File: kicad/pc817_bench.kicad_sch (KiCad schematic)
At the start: 27 parts, among them J1 24V, e-stops, lidars, U1 PC817, U2 PC817, U3 PC817, U4 PC817

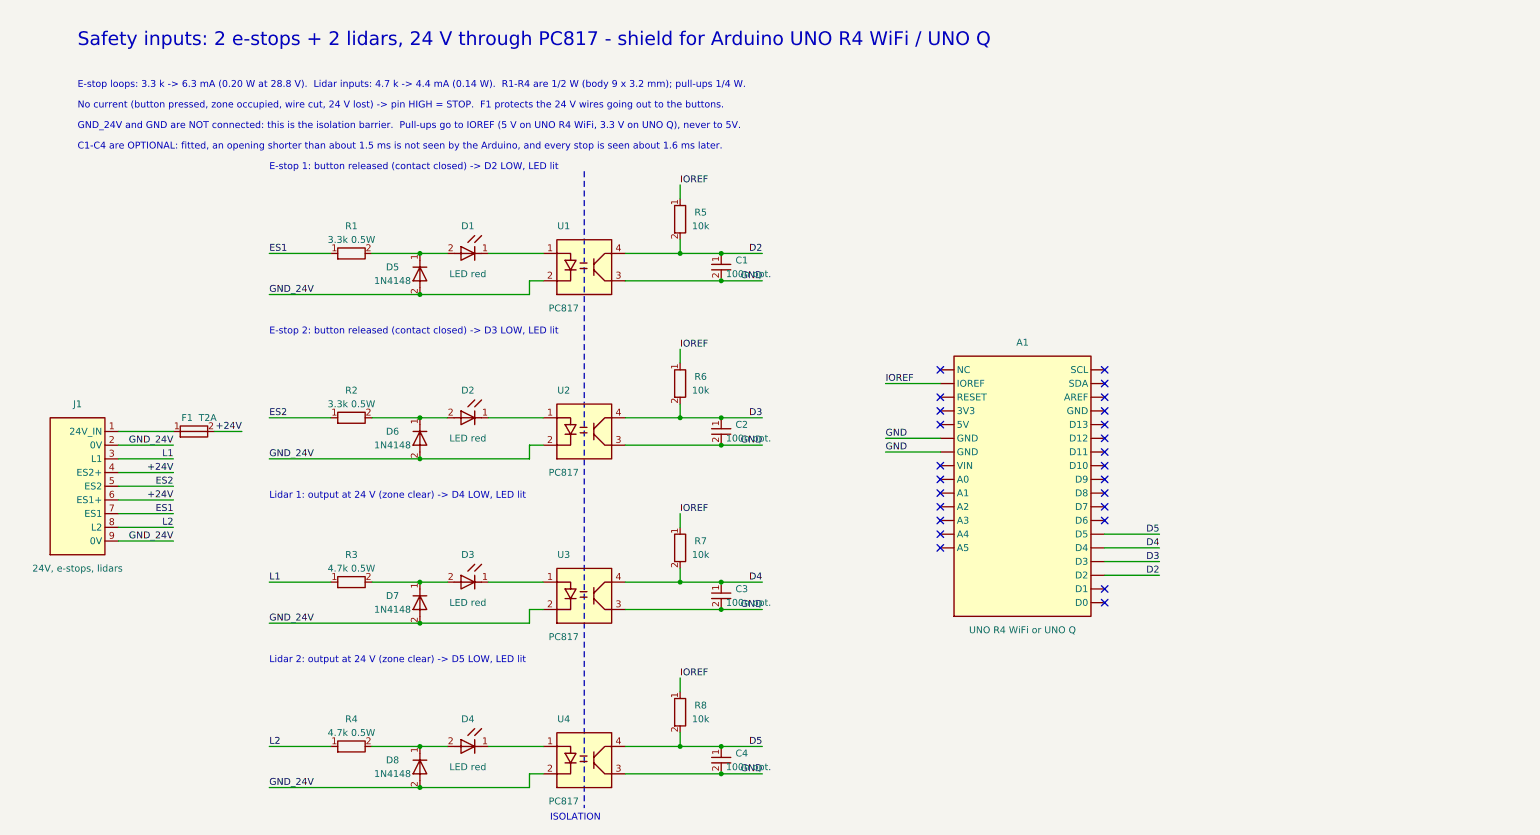
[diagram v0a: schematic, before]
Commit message: Schematic: draw the two external e-stop buttons and how they wire to the terminals
S1 (front) between ES1+ and ES1, S2 (rear) between ES2+ and ES2, in a dashed
box marked as external. Graphics only: no change to the netlist or the board.
The sheet content is shifted right to make room.

Co-Authored-By: Claude Fable 5.1 <noreply@anthropic.com>
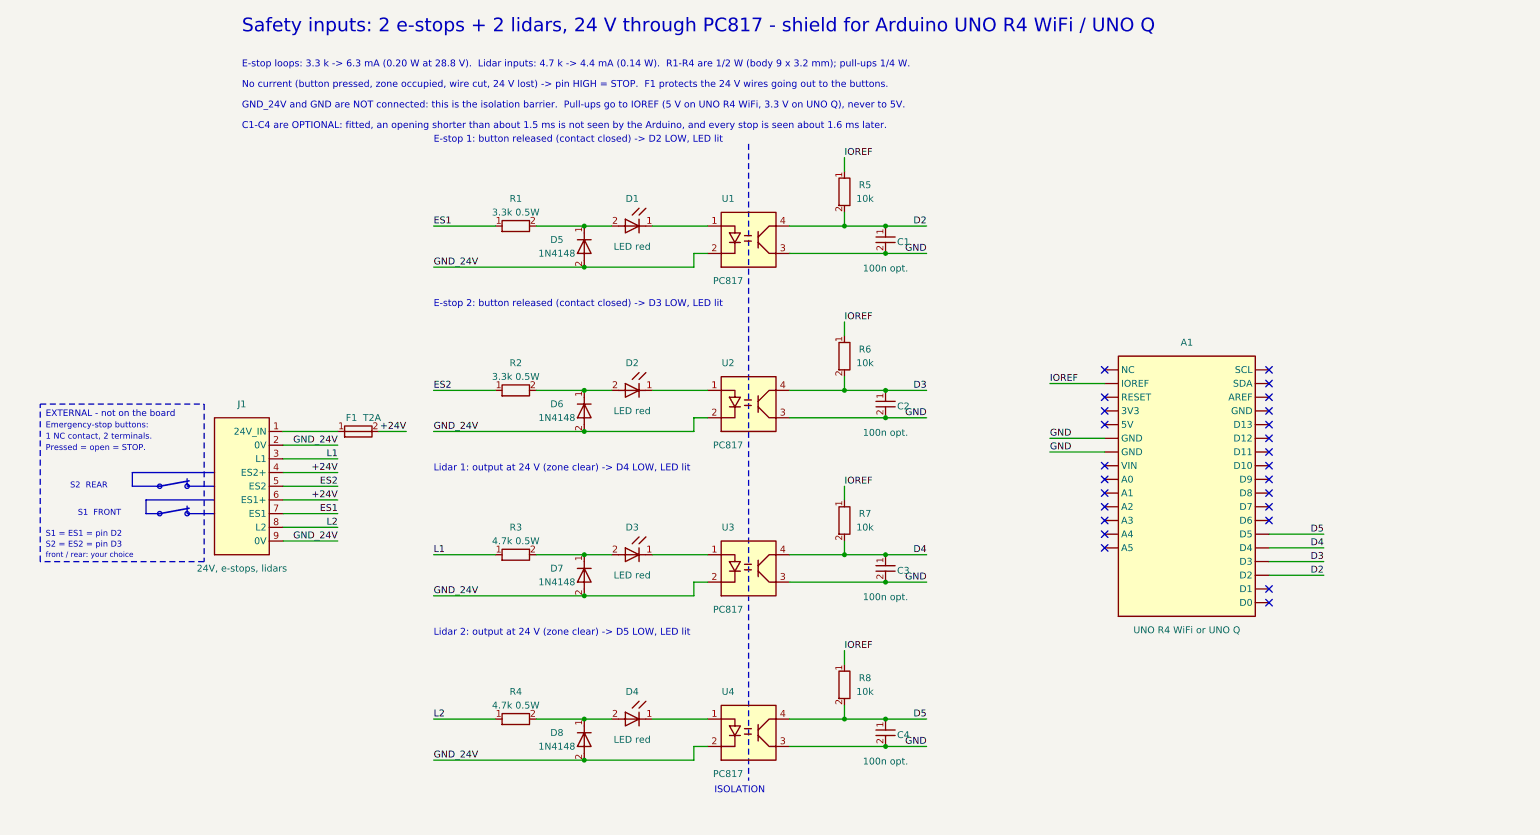
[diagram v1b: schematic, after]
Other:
- note added: "1 NC contact, 2 terminals."
- note added: "EXTERNAL - not on the board"
- note added: "Emergency-stop buttons:"
- note added: "Pressed = open = STOP."
- note added: "S1 = ES1 = pin D2"
- note added: "S1 FRONT"
- note added: "S2 = ES2 = pin D3"
- note added: "S2 REAR"
- note added: "front / rear: your choice"
- moved on the sheet: C1, C2, C3, C4, D1, D2, D3, D4, D5, D6, D7, D8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

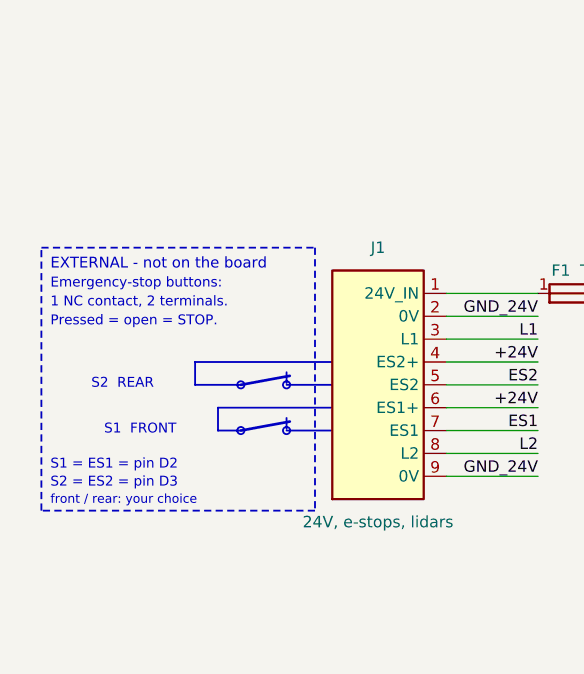
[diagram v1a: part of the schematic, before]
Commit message: Schematic: draw the external 24 V source and where it connects (24V and 0V screws)
Co-Authored-By: Claude Fable 5.1 <noreply@anthropic.com>
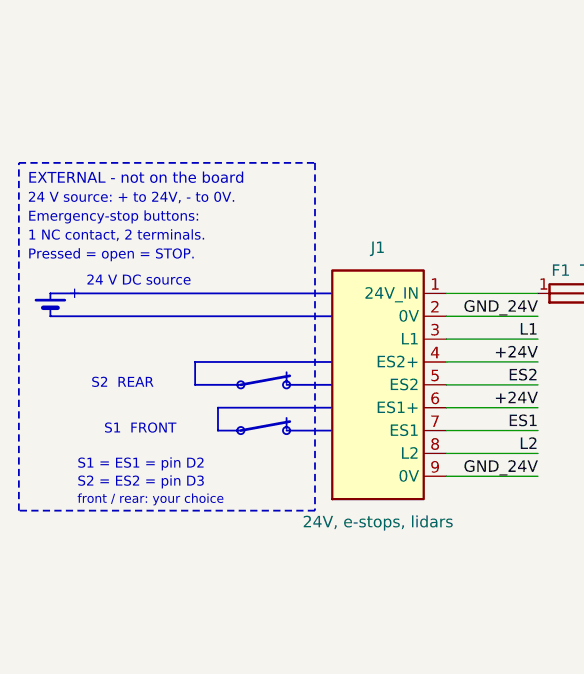
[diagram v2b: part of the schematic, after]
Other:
- note added: "+"
- note added: "24 V DC source"
- note added: "24 V source: + to 24V, - to 0V."
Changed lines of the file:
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@@
   (wire (pts (xy 63.5 121.92) (xy 73.66 121.92)) (stroke (width 0) (type default)))
   (label "GND_24V" (at 73.66 121.92 0) (effects (font (size 1.27 1.27)) (justify right bottom)))
+  (polyline (pts (xy 50.8 101.6) (xy 19.48 101.6) (xy 19.48 102.35)) (stroke (width 0.2) (type default)))
+  (polyline (pts (xy 17.88 102.35) (xy 21.08 102.35)) (stroke (width 0.3) (type default)))
+  (polyline (pts (xy 18.68 103.2) (xy 20.28 103.2)) (stroke (width 0.5) (type default)))
+  (polyline (pts (xy 19.48 103.2) (xy 19.48 104.14) (xy 50.8 104.14)) (stroke (width 0.2) (type default)))
+  (text "+" (at 21.48 102.5 0) (effects (font (size 1.2 1.2)) (justify left bottom)))
+  (text "24 V DC source" (at 23.48 101 0) (effects (font (size 1.1 1.1)) (justify left bottom)))
   (polyline (pts (xy 50.8 116.84) (xy 45.72 116.84)) (stroke (width 0.2) (type default)))
   (circle (center 45.72 116.84) (radius 0.4) (stroke (width 0.2) (type default)) (fill (type none)))
@@
   (polyline (pts (xy 40.64 111.76) (xy 35.56 111.76) (xy 35.56 109.22) (xy 50.8 109.22)) (stroke (width 0.2) (type default)))
   (text "S2  REAR" (at 30.98 112.36 0) (effects (font (size 1.1 1.1)) (justify right bottom)))
-  (polyline (pts (xy 18.48 96.52) (xy 48.88 96.52) (xy 48.88 125.74) (xy 18.48 125.74) (xy 18.48 96.52)) (stroke (width 0.2) (type dash)))
-  (text "EXTERNAL - not on the board" (at 19.48 99.12 0) (effects (font (size 1.2 1.2)) (justify left bottom)))
-  (text "Emergency-stop buttons:" (at 19.48 101.22 0) (effects (font (size 1.1 1.1)) (justify left bottom)))
-  (text "1 NC contact, 2 terminals." (at 19.48 103.32 0) (effects (font (size 1.1 1.1)) (justify left bottom)))
-  (text "Pressed = open = STOP." (at 19.48 105.42 0) (effects (font (size 1.1 1.1)) (justify left bottom)))
-  (text "S1 = ES1 = pin D2" (at 19.48 121.34 0) (effects (font (size 1.1 1.1)) (justify left bottom)))
-  (text "S2 = ES2 = pin D3" (at 19.48 123.34 0) (effects (font (size 1.1 1.1)) (justify left bottom)))
-  (text "front / rear: your choice" (at 19.48 125.24 0) (effects (font (size 1 1)) (justify left bottom)))
+  (polyline (pts (xy 15.98 87.1) (xy 48.88 87.1) (xy 48.88 125.74) (xy 15.98 125.74) (xy 15.98 87.1)) (stroke (width 0.2) (type dash)))
+  (text "EXTERNAL - not on the board" (at 16.98 89.7 0) (effects (font (size 1.2 1.2)) (justify left bottom)))
+  (text "24 V source: + to 24V, - to 0V." (at 16.98 91.8 0) (effects (font (size 1.1 1.1)) (justify left bottom)))
+  (text "Emergency-stop buttons:" (at 16.98 93.9 0) (effects (font (size 1.1 1.1)) (justify left bottom)))
+  (text "1 NC contact, 2 terminals." (at 16.98 96 0) (effects (font (size 1.1 1.1)) (justify left bottom)))
+  (text "Pressed = open = STOP." (at 16.98 98.1 0) (effects (font (size 1.1 1.1)) (justify left bottom)))
+  (text "S1 = ES1 = pin D2" (at 22.48 121.34 0) (effects (font (size 1.1 1.1)) (justify left bottom)))
+  (text "S2 = ES2 = pin D3" (at 22.48 123.34 0) (effects (font (size 1.1 1.1)) (justify left bottom)))
+  (text "front / rear: your choice" (at 22.48 125.24 0) (effects (font (size 1 1)) (justify left bottom)))
   (symbol (lib_id "bench:UNO_R4_WIFI") (at 231.14 111.76 0) (unit 1) (in_bom yes) (on_board yes) (dnp no)
     (property "Reference" "A1" (at 231.14 85.09 0) (effects (font (size 1.27 1.27))))
